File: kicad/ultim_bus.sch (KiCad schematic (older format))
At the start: 12 parts, among them P1 CONN_1, P10 CONN_1, P11 CONN_1, P12 CONN_1, P2 CONN_1, P3 CONN_1, P4 CONN_1, P5 CONN_1, P6 CONN_1, P7 CONN_1, P8 CONN_1, P9 CONN_1

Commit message: UlTiM8x8 board layout complete, Gerbers ready for fab
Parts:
- added L1, L2, L3, L4: OSHW, ultim8x8_libs:OSHW_6mm, symbol CONN_1
- added L10, L11, L12, L9: Maniacal, ultim8x8_libs:logo_MLlabs_small, symbol CONN_1
- added L13, L14, L15, L16: ULTiM, ultim8x8_libs:logo_ultim8x8_small, symbol CONN_1
- added L5, L6, L7, L8: WyoLum, ultim8x8_libs:logo_wyo_butterfly_small, symbol CONN_1
- added P13, P14, P15, P16, P17, P18, P19, P20, P21, P22, P23, P24, P25, P26, P27, P28, P29, P30, P31, P32, P33, P34, P35, P36, P37, P38, P39, P40, P41, P42, P43, P44, P45, P46, P47, P48, P49, P50, P51, P52, P53, P54, P55, P56, P57, P58, P59, P60, P61, P62, P63, P64, P65, P66: CONN_1, ultim8x8_libs:Screw, symbol CONN_1
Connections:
- new net: P13.1, P14.1, P15.1, P16.1, P17.1, P18.1, P19.1, P20.1, P21.1, P22.1, P23.1, P24.1
- new net: P31.1, P32.1, P33.1, P34.1, P35.1, P36.1, P37.1, P38.1, P39.1, P40.1, P41.1, P42.1
- new net: P49.1, P50.1, P51.1, P52.1, P53.1, P54.1, P55.1, P56.1, P57.1, P58.1, P59.1, P60.1
- no-connect marks 0 -> 34

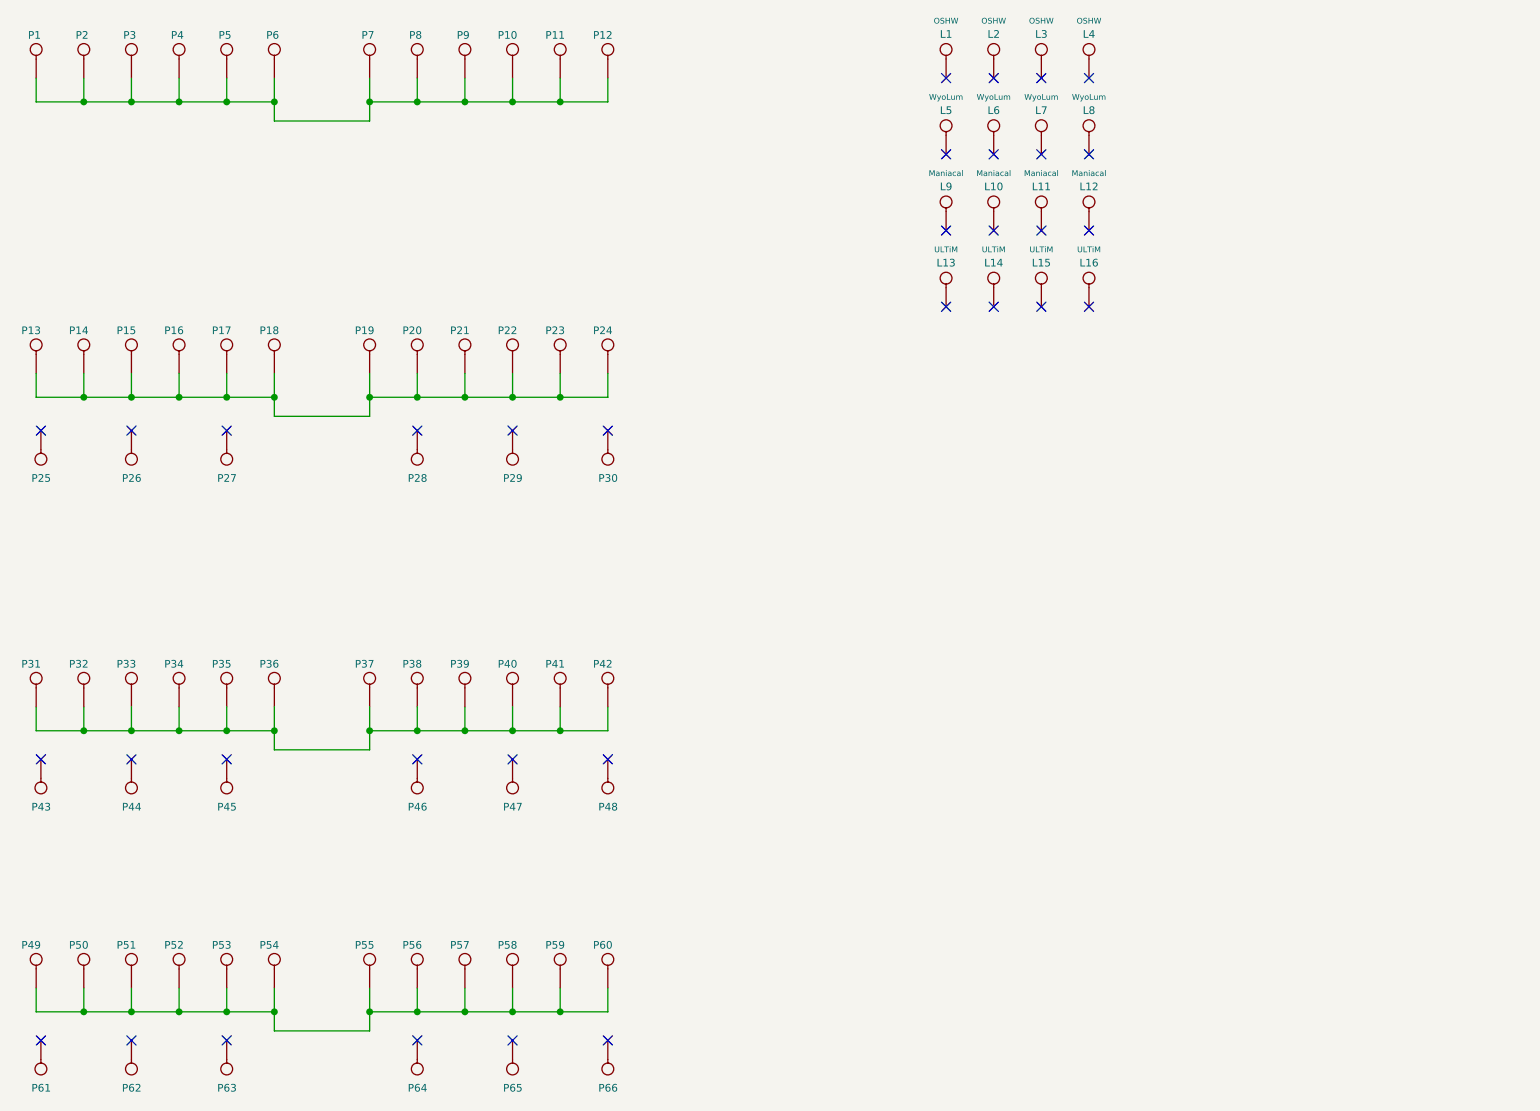
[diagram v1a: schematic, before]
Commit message: UlTiM_bus layout, gerber complete. Bus accessory for ULTiM8x8
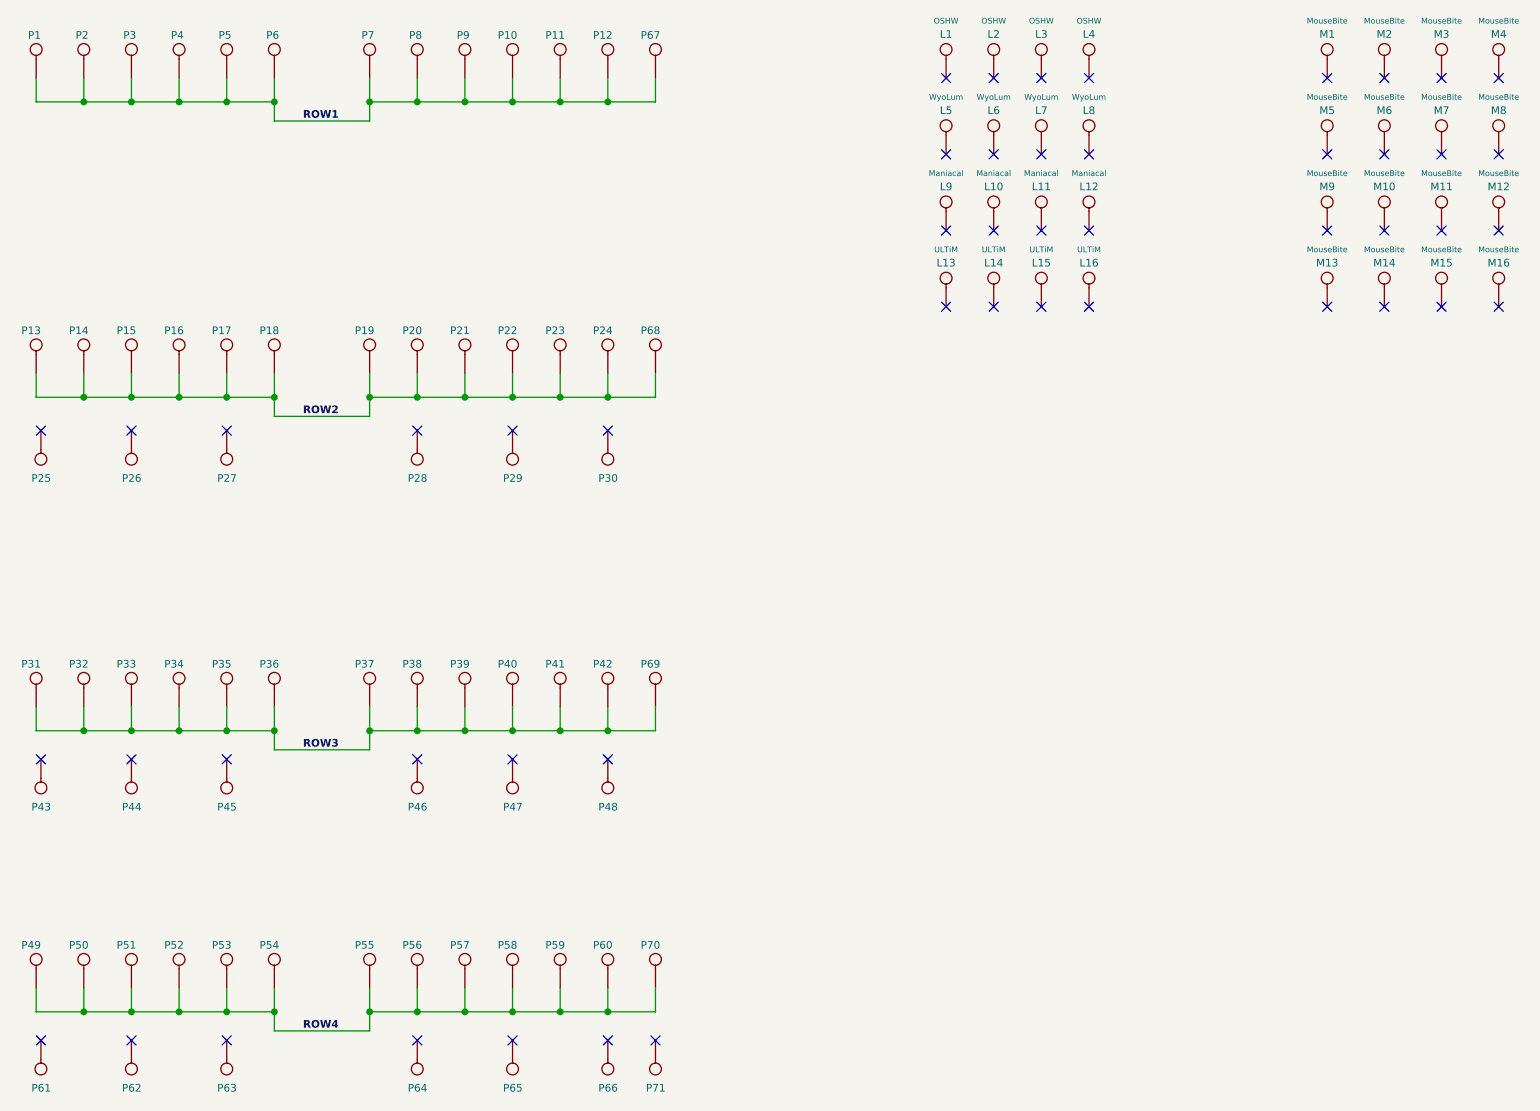
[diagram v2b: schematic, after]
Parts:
- added M1, M10, M11, M12, M13, M14, M15, M16, M2, M3, M4, M5, M6, M7, M8, M9: MouseBite, ultim8x8_libs:mouse-bite-2.54mm-slot, symbol CONN_1
- added P67, P68, P69, P70, P71: CONN_1, ultim8x8_libs:Screw, symbol CONN_1
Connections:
- net ROW1: now reaches P1.1, P10.1, P11.1, P12.1, P2.1, P3.1, P4.1, P5.1, P6.1, P7.1, P8.1, P9.1
- net ROW1: now also P67.1
- net ROW2: now reaches P13.1, P14.1, P15.1, P16.1, P17.1, P18.1, P19.1, P20.1, P21.1, P22.1, P23.1, P24.1
- net ROW2: now also P68.1
- net ROW3: now reaches P31.1, P32.1, P33.1, P34.1, P35.1, P36.1, P37.1, P38.1, P39.1, P40.1, P41.1, P42.1
- net ROW3: now also P69.1
- net ROW4: now reaches P49.1, P50.1, P51.1, P52.1, P53.1, P54.1, P55.1, P56.1, P57.1, P58.1, P59.1, P60.1
- net ROW4: now also P70.1
- no-connect marks 34 -> 51
